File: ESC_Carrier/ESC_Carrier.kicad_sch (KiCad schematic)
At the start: 21 parts, among them J10 Molex 430450821, J11 Molex 43045-0627, J12 Molex 43045-0627, J13 Molex 43045-0627, J14 Molex 43045-0627, J15 Molex 43045-0627, J16 Molex 43045-0627, J17 Molex 43045-0627, J18 Molex 43045-0627, J9 Molex 53047-0510

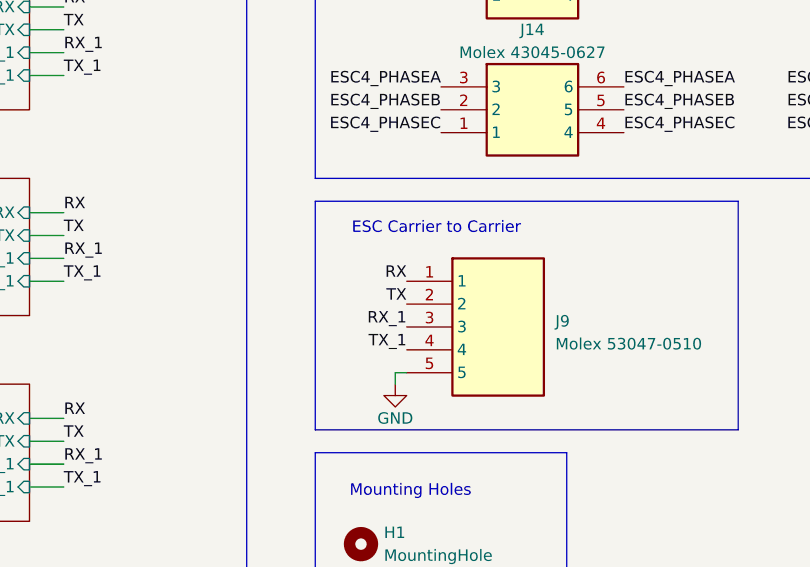
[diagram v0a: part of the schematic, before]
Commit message: Fix: updated uart connections to carrier board
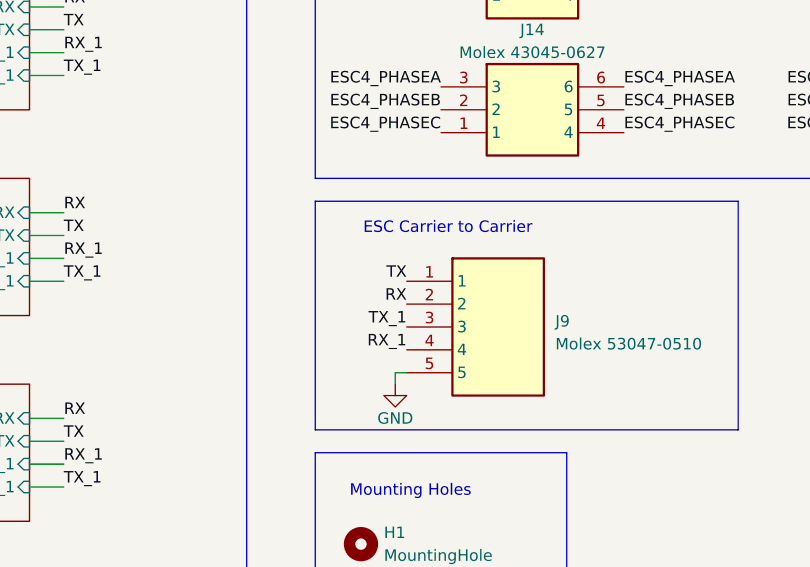
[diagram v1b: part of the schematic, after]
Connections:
- net RX: now also J9.2; no longer J9.1
- net RX_1: now also J9.4; no longer J9.3
- net TX: now also J9.1; no longer J9.2
- net TX_1: now also J9.3; no longer J9.4
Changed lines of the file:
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@@
   )
   (text "ESC Carrier to Carrier\n" (exclude_from_sim no)
- (at 132.08 93.98 0)
+ (at 133.35 93.98 0)
     (effects (font (size 1.27 1.27)) (justify right bottom))
   )
@@
     (effects (font (size 1.27 1.27)) (justify left bottom))
   )
-  (label "RX" (at 119.38 99.06 180) (fields_autoplaced)
+  (label "TX" (at 119.38 99.06 180) (fields_autoplaced)
     (effects (font (size 1.27 1.27)) (justify right bottom))
   )
@@
     (effects (font (size 1.27 1.27)) (justify right bottom))
   )
-  (label "RX_1" (at 119.38 104.14 180) (fields_autoplaced)
+  (label "TX_1" (at 119.38 104.14 180) (fields_autoplaced)
     (effects (font (size 1.27 1.27)) (justify right bottom))
   )
@@
     (effects (font (size 1.27 1.27)) (justify right bottom))
   )
-  (label "TX_1" (at 119.38 106.68 180) (fields_autoplaced)
+  (label "RX_1" (at 119.38 106.68 180) (fields_autoplaced)
     (effects (font (size 1.27 1.27)) (justify right bottom))
   )
@@
     (effects (font (size 1.27 1.27)) (justify right bottom))
   )
-  (label "TX" (at 119.38 101.6 180) (fields_autoplaced)
-    (effects (font (size 1.27 1.27)) (justify right bottom))
-  )
+  (label "RX" (at 119.38 101.6 180) (fields_autoplaced)
+    (effects (font (size 1.27 1.27)) (justify right bottom))
+  )

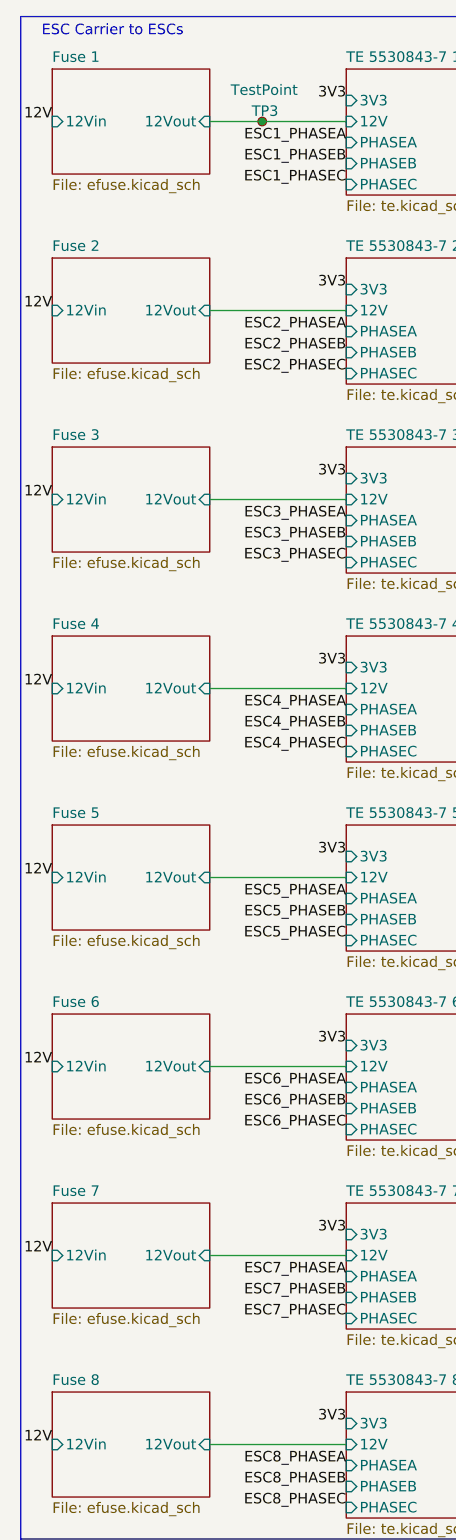
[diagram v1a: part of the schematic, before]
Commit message: Feat: added ntc thermistor
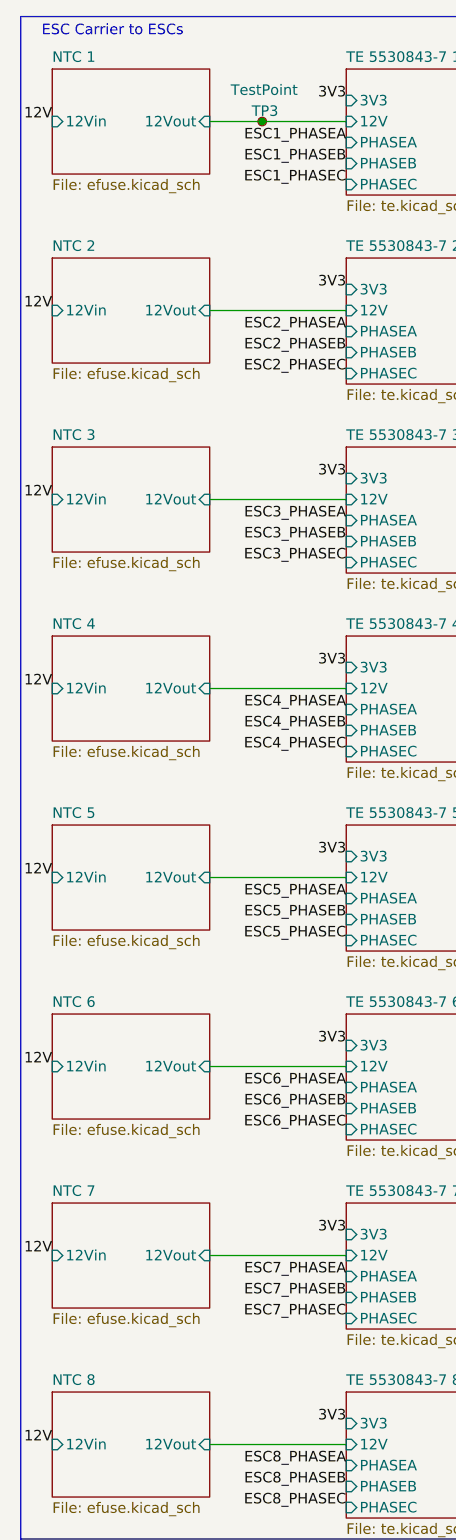
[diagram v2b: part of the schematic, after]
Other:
- sheet Fuse 1 renamed NTC 1
- sheet Fuse 2 renamed NTC 2
- sheet Fuse 3 renamed NTC 3
- sheet Fuse 4 renamed NTC 4
- sheet Fuse 5 renamed NTC 5
- sheet Fuse 6 renamed NTC 6
- sheet Fuse 7 renamed NTC 7
- sheet Fuse 8 renamed NTC 8
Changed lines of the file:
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@@
     (stroke (width 0.1524) (type solid))
     (fill (color 0 0 0 0.0000))
-    (property "Sheetname" "Fuse 3" (at 21.59 64.0584 0)
+    (property "Sheetname" "NTC 3" (at 21.59 64.0584 0)
       (effects (font (size 1.27 1.27)) (justify left bottom))
     )
@@
     (stroke (width 0.1524) (type solid))
     (fill (color 0 0 0 0.0000))
-    (property "Sheetname" "Fuse 8" (at 21.59 178.3584 0)
+    (property "Sheetname" "NTC 8" (at 21.59 178.3584 0)
       (effects (font (size 1.27 1.27)) (justify left bottom))
     )
@@
     (stroke (width 0.1524) (type solid))
     (fill (color 0 0 0 0.0000))
-    (property "Sheetname" "Fuse 1" (at 21.59 18.3384 0)
+    (property "Sheetname" "NTC 1" (at 21.59 18.3384 0)
       (effects (font (size 1.27 1.27)) (justify left bottom))
     )
@@
     (stroke (width 0.1524) (type solid))
     (fill (color 0 0 0 0.0000))
-    (property "Sheetname" "Fuse 5" (at 21.59 109.7784 0)
+    (property "Sheetname" "NTC 5" (at 21.59 109.7784 0)
       (effects (font (size 1.27 1.27)) (justify left bottom))
     )
@@
     (stroke (width 0.1524) (type solid))
     (fill (color 0 0 0 0.0000))
-    (property "Sheetname" "Fuse 4" (at 21.59 86.9184 0)
+    (property "Sheetname" "NTC 4" (at 21.59 86.9184 0)
       (effects (font (size 1.27 1.27)) (justify left bottom))
     )
@@
     (stroke (width 0.1524) (type solid))
     (fill (color 0 0 0 0.0000))
-    (property "Sheetname" "Fuse 7" (at 21.59 155.4984 0)
+    (property "Sheetname" "NTC 7" (at 21.59 155.4984 0)
       (effects (font (size 1.27 1.27)) (justify left bottom))
     )
@@
     (stroke (width 0.1524) (type solid))
     (fill (color 0 0 0 0.0000))
-    (property "Sheetname" "Fuse 2" (at 21.59 41.1984 0)
+    (property "Sheetname" "NTC 2" (at 21.59 41.1984 0)
       (effects (font (size 1.27 1.27)) (justify left bottom))
     )
@@
     (stroke (width 0.1524) (type solid))
     (fill (color 0 0 0 0.0000))
-    (property "Sheetname" "Fuse 6" (at 21.59 132.6384 0)
-      (effects (font (size 1.27 1.27)) (justify left bottom))
-    )
+    (property "Sheetname" "NTC 6" (at 21.59 132.6384 0)
+      (effects (font (size 1.27 1.27)) (justify left bottom))
+    )

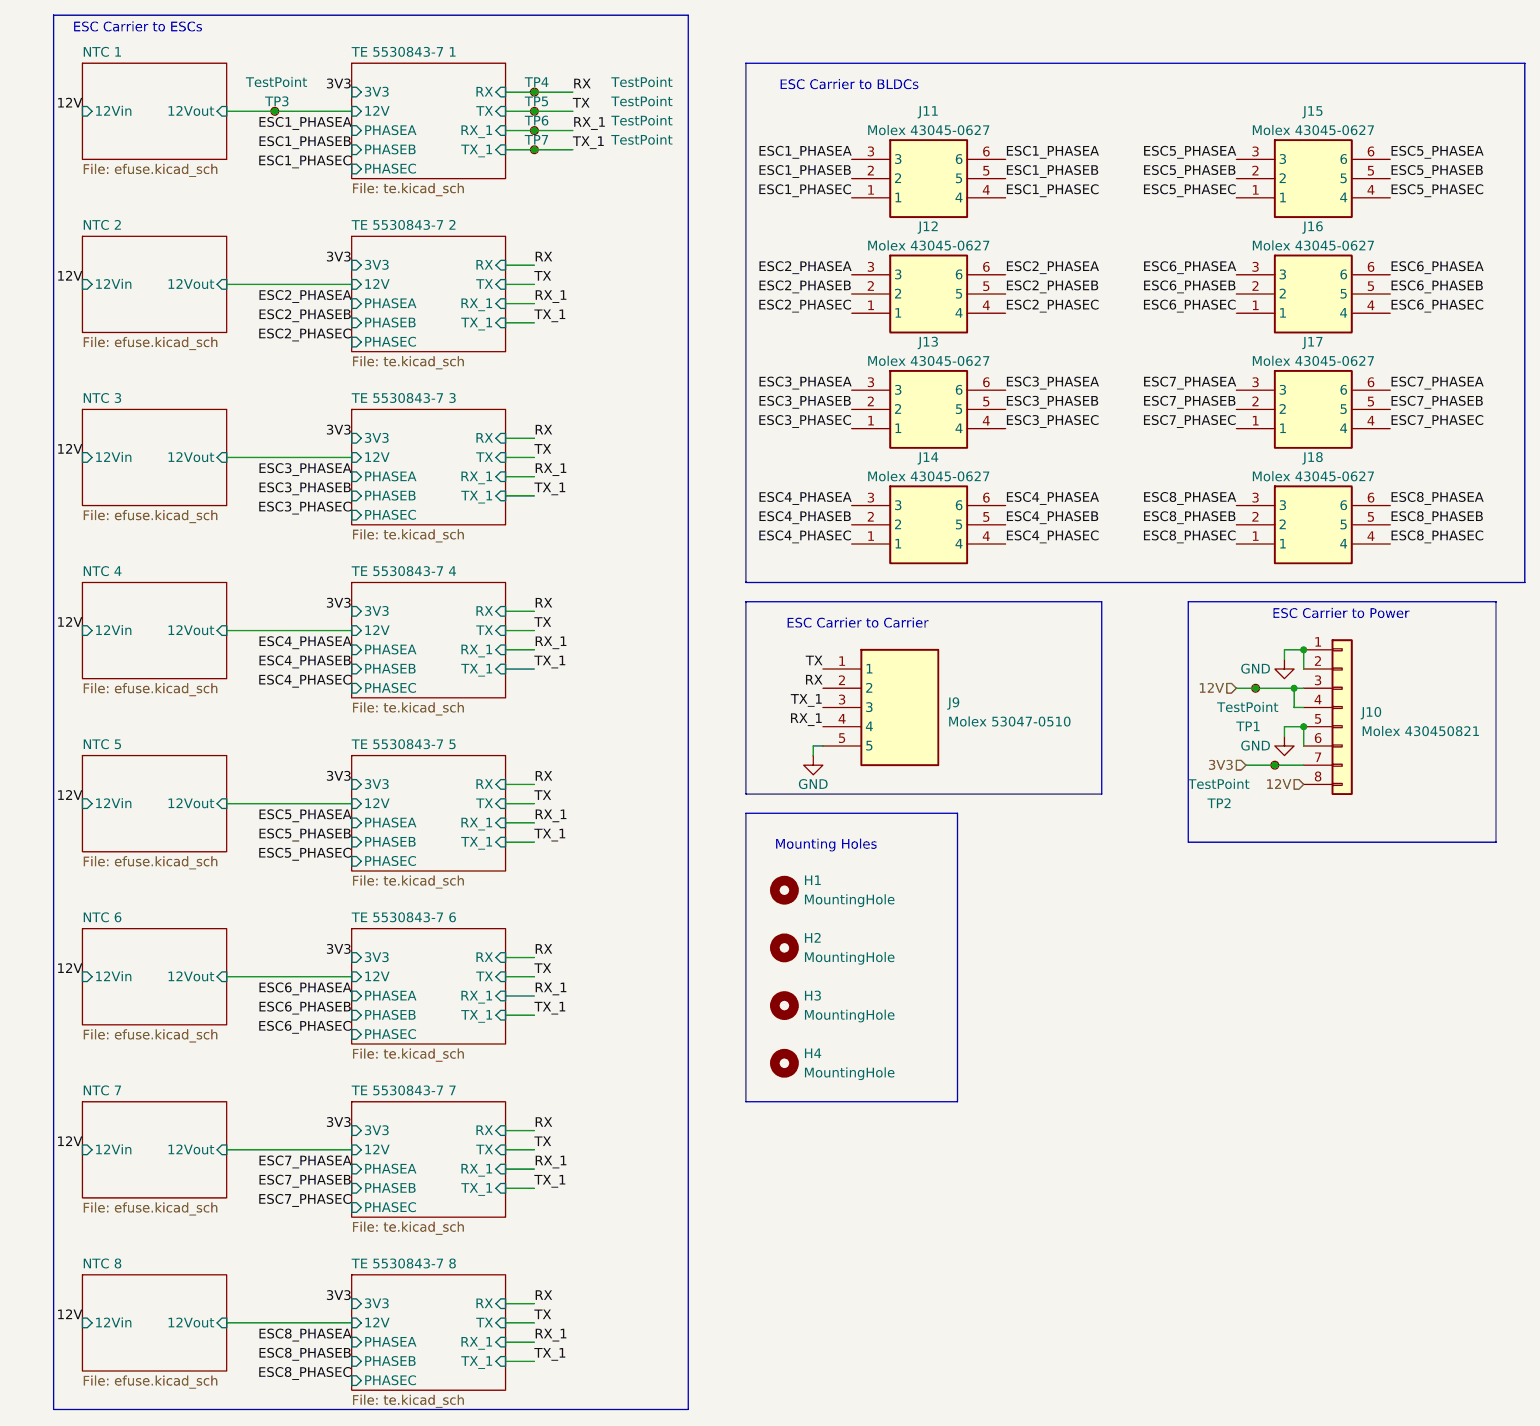
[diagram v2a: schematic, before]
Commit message: Feat: removed 7 ntc thermistors
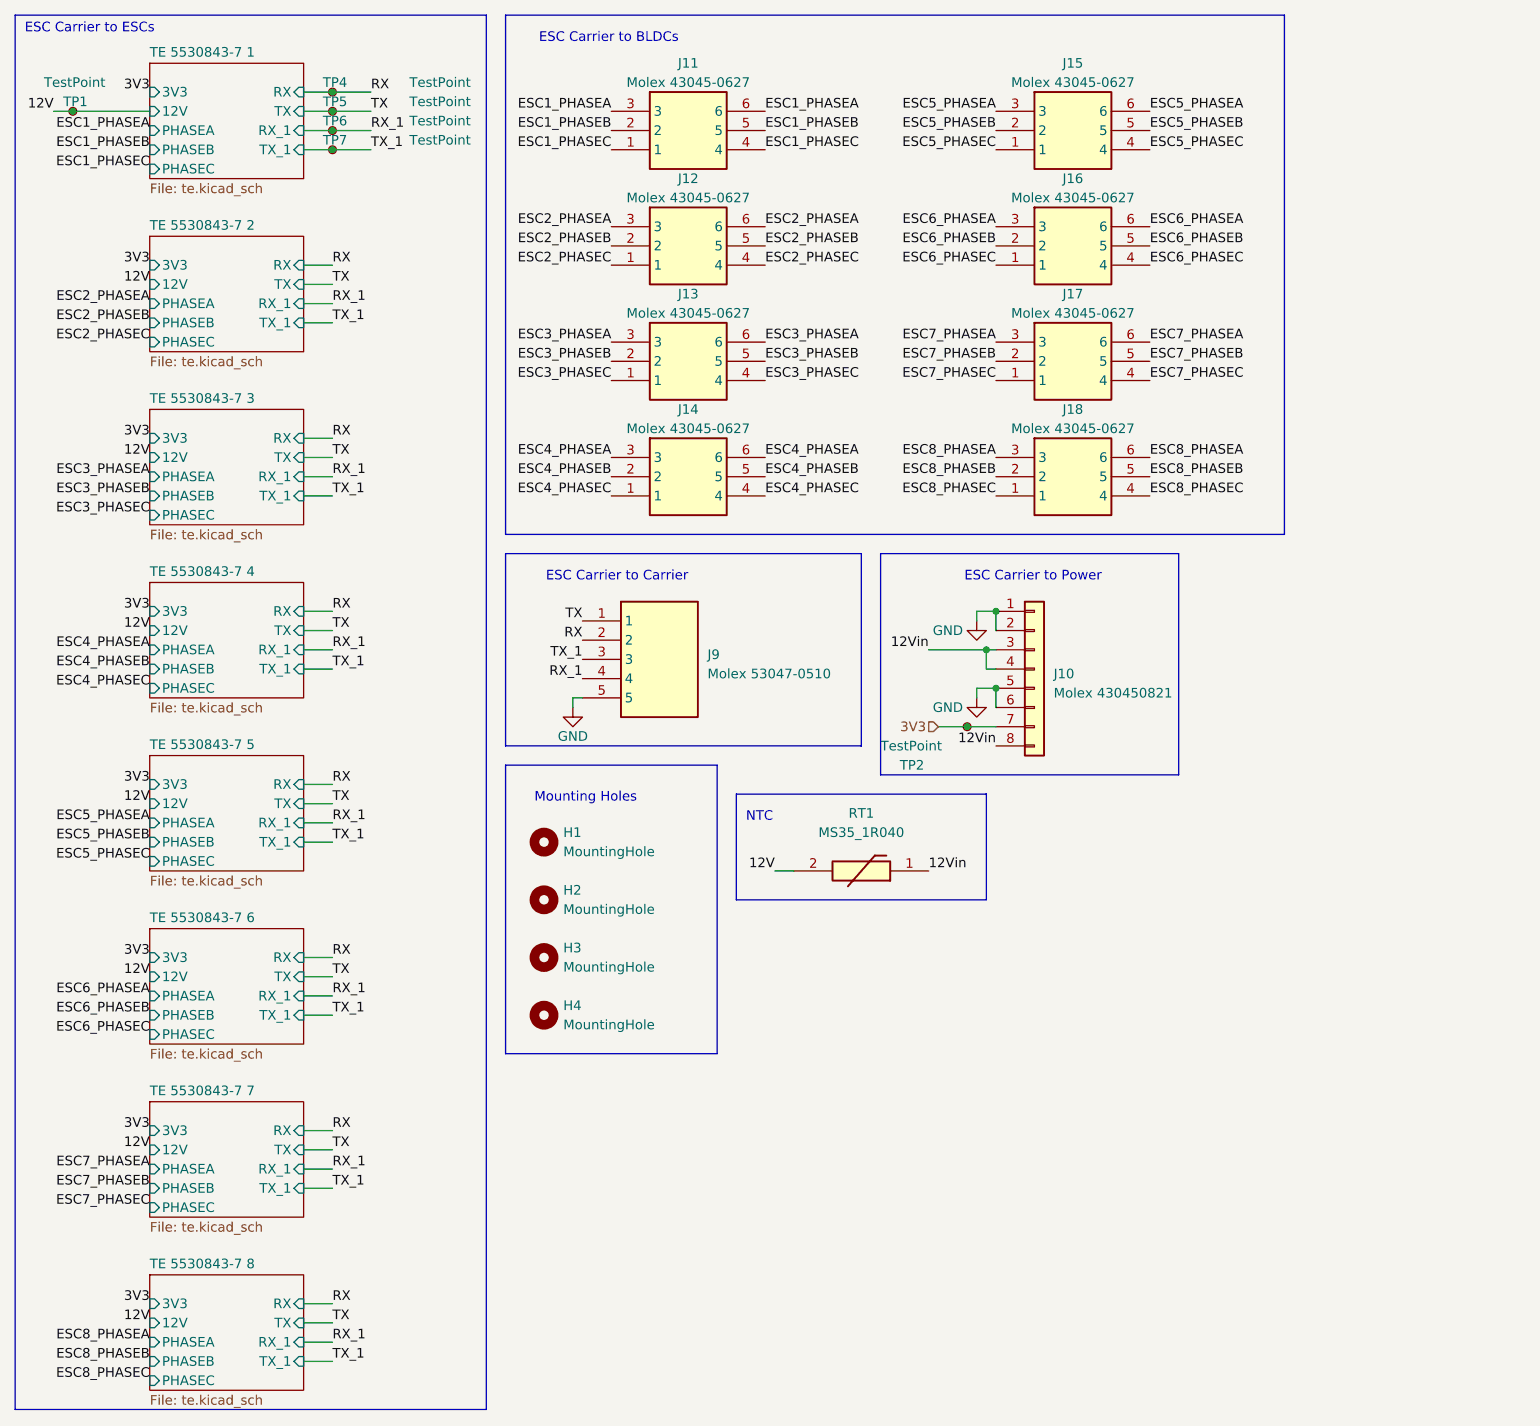
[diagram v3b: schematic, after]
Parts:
- removed TP1: TestPoint, TestPoint:TestPoint_Pad_D2.0mm, symbol Connector:TestPoint_Small
- added RT1: MS35_1R040, MS351R040, symbol MS35_1R040:MS35_1R040
- renumbered TP3 to TP1
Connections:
- net NTC 1/12Vout is gone; now on net 12V: TP1.1
- net 12V: now also RT1.2; no longer J10.3 (Pin_3), J10.4 (Pin_4), J10.8 (Pin_8)
- new net 12Vin: J10.3 (Pin_3), J10.4 (Pin_4), J10.8 (Pin_8), RT1.1
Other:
- removed sheet NTC 1
- removed sheet NTC 2
- removed sheet NTC 3
- removed sheet NTC 4
- removed sheet NTC 5
- removed sheet NTC 6
- removed sheet NTC 7
- removed sheet NTC 8
- note added: "NTC"
- moved on the sheet: H1, H2, H3, H4, J10, J11, J12, J13, J14, J15, J16, J17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
